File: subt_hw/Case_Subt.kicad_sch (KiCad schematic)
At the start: 44 parts, among them J1 P2.00 01x04, J2 USB_C_Receptacle_USB2.0_14P, J3 Conn_01x02, U1 RP2040, U2 W25Q16JVUXIQ, U3 MT2492, U4 SPX3819M5-L-3-3, U5 USBLC6-2SC6, Y1 12MHz

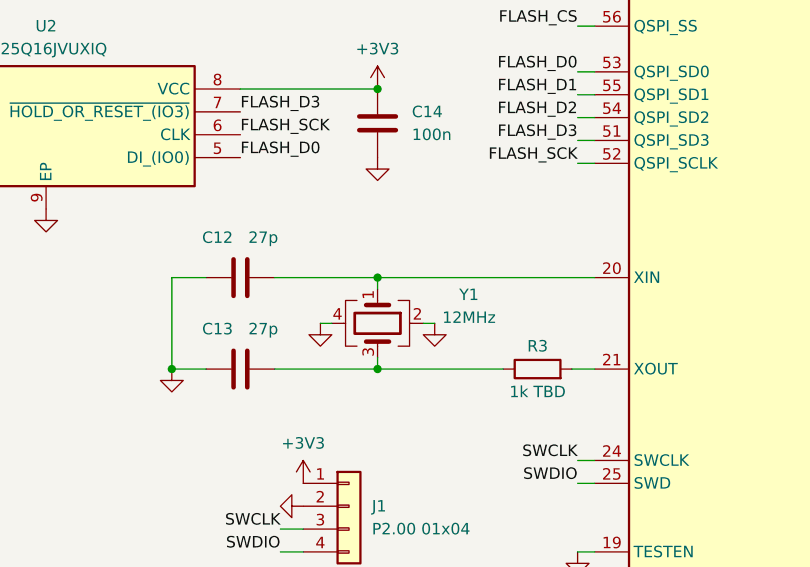
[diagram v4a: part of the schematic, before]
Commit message: Update subtree hardware with actual values in assembly
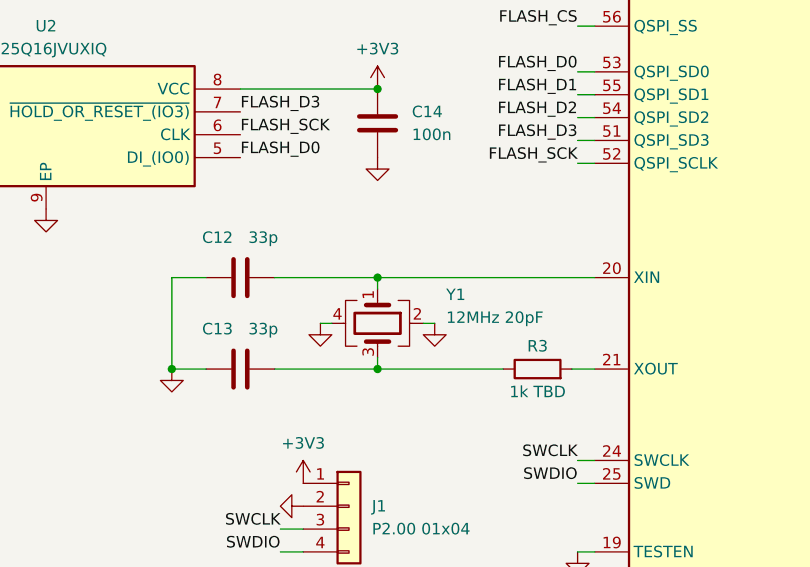
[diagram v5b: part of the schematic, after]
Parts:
- C12, C13: value 27p -> 33p
- Y1: value 12MHz -> 12MHz 20pF
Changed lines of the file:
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@@
       (effects (font (size 1.27 1.27)))
     )
-    (property "Value" "27p" (at 95.25 99.695 90)
+    (property "Value" "33p" (at 95.25 99.695 90)
       (effects (font (size 1.27 1.27)))
     )
@@
   (symbol (lib_id "Device:Crystal_GND24") (at 107.95 99.06 270) (unit 1)
     (in_bom yes) (on_board yes) (dnp no)
-    (property "Reference" "Y1" (at 118.11 95.885 90)
-      (effects (font (size 1.27 1.27)))
-    )
-    (property "Value" "12MHz" (at 118.11 98.425 90)
-      (effects (font (size 1.27 1.27)))
+    (property "Reference" "Y1" (at 115.57 95.885 90)
+      (effects (font (size 1.27 1.27)) (justify left))
+    )
+    (property "Value" "12MHz 20pF" (at 115.57 98.425 90)
+      (effects (font (size 1.27 1.27)) (justify left))
     )
     (property "Footprint" "Crystal:Crystal_SMD_3225-4Pin_3.2x2.5mm" (at 107.95 99.06 0)
@@
       (effects (font (size 1.27 1.27)))
     )
-    (property "Value" "27p" (at 95.25 89.535 90)
-      (effects (font (size 1.27 1.27)))
-    )
+    (property "Value" "33p" (at 95.25 89.535 90)
+      (effects (font (size 1.27 1.27)))
+    )

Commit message: Update unit hardware document with actual values in assembly
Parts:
- C16: value 22n -> 100n
- R5: value 100k -> 130k
- R6: value 22k -> 24k
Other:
- note added: "FB ref. 0.8 V typ. (MP2369DJ)"
- note added: "Set output = 5.13 V"
- note removed: "FB ref. 0.6 V typ."
- note removed: "Set output = 3.32 V"
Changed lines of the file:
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@@
     (effects (font (size 1.27 1.27) italic) (justify left bottom))
   )
-  (text "Set output = 3.32 V" (at 65.405 30.48 0)
+  (text "Set output = 5.13 V" (at 65.405 30.48 0)
     (effects (font (size 1.27 1.27) italic) (justify left bottom))
   )
@@
     (effects (font (size 1.27 1.27) italic) (justify left bottom))
   )
-  (text "FB ref.\n0.6 V typ." (at 48.26 44.45 0)
+  (text "FB ref.\n0.8 V typ.\n(MP2369DJ)" (at 48.26 46.355 0)
     (effects (font (size 1.27 1.27) italic) (justify left bottom))
   )
@@
       (effects (font (size 1.27 1.27)) (justify left))
     )
-    (property "Value" "22k" (at 62.865 44.45 0)
+    (property "Value" "24k" (at 62.865 44.45 0)
       (effects (font (size 1.27 1.27)) (justify left))
     )
@@
       (effects (font (size 1.27 1.27)) (justify left))
     )
-    (property "Value" "100k" (at 62.865 36.83 0)
+    (property "Value" "130k" (at 62.865 36.83 0)
       (effects (font (size 1.27 1.27)) (justify left))
     )
@@
       (effects (font (size 1.27 1.27)))
     )
-    (property "Value" "22n" (at 47.625 20.955 90)
-      (effects (font (size 1.27 1.27)))
-    )
+    (property "Value" "100n" (at 47.625 20.955 90)
+      (effects (font (size 1.27 1.27)))
+    )
